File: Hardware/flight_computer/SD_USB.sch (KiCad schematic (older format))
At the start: 10 parts

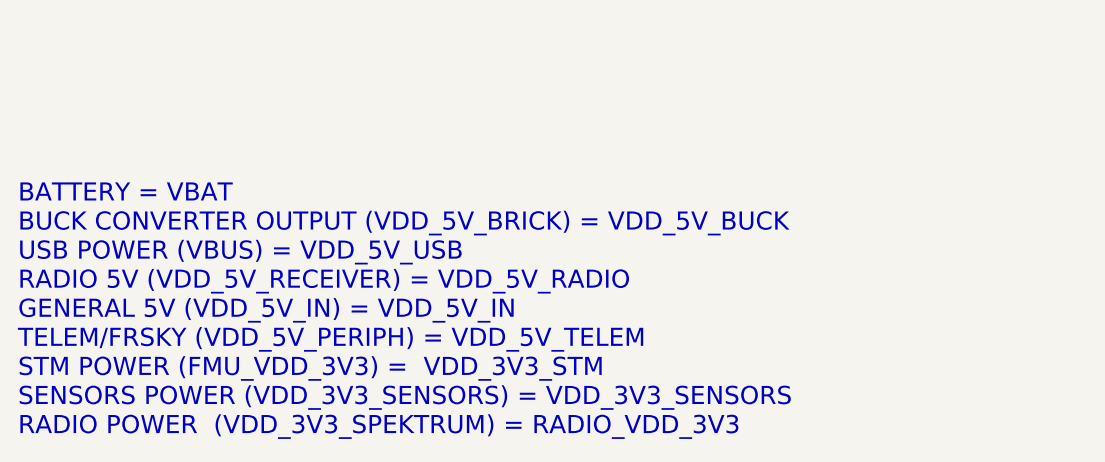
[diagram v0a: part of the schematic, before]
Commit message: added more components, added buzzer, servo circuits, re-arranged some power
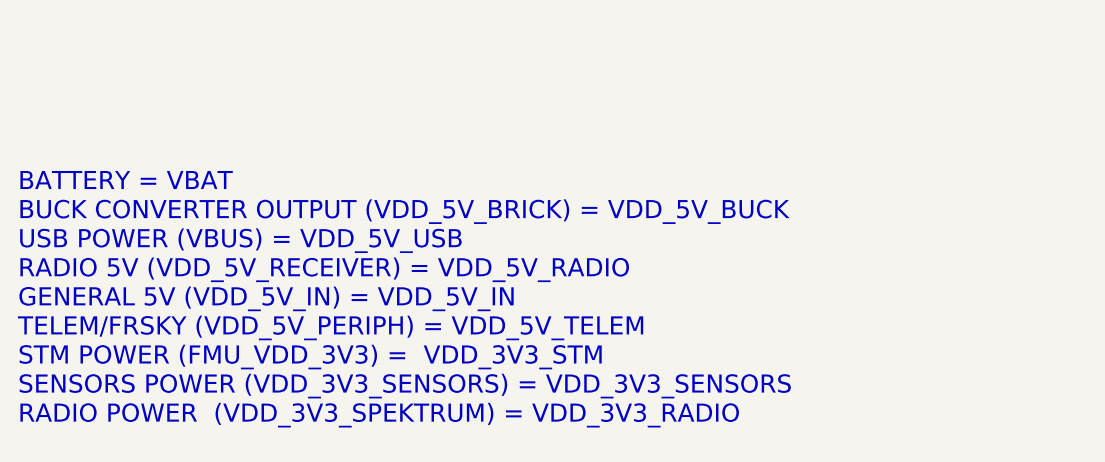
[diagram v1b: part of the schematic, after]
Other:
- note added: "BATTERY = VBAT\nBUCK CONVERTER OUTPUT (VDD_5V_BRICK) = VDD_5V_BUCK\nUSB POWER (VBUS) = VDD_5V_USB\nRADIO 5V (VDD_5V_RECEIVER) = VDD_5V_RADIO\nGENERAL 5V (VDD_5V_IN) = VDD_5V_IN\nTELEM/FRSKY (VDD_5V_PERIPH) = VDD_5V_TELEM\nSTM POWER (FMU_VDD_3V3) = VDD_3V3_STM\nSENSORS POWER (VDD_3V3_SENSORS) = VDD_3V3_SENSORS\nRADIO POWER (VDD_3V3_SPEKTRUM) = VDD_3V3_RADIO\n"
- note removed: "BATTERY = VBAT\nBUCK CONVERTER OUTPUT (VDD_5V_BRICK) = VDD_5V_BUCK\nUSB POWER (VBUS) = VDD_5V_USB\nRADIO 5V (VDD_5V_RECEIVER) = VDD_5V_RADIO\nGENERAL 5V (VDD_5V_IN) = VDD_5V_IN\nTELEM/FRSKY (VDD_5V_PERIPH) = VDD_5V_TELEM\nSTM POWER (FMU_VDD_3V3) = VDD_3V3_STM\nSENSORS POWER (VDD_3V3_SENSORS) = VDD_3V3_SENSORS\nRADIO POWER (VDD_3V3_SPEKTRUM) = RADIO_VDD_3V3\n"
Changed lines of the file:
@@
 $Descr A4 11693 8268
 encoding utf-8
-Sheet 3 5
+Sheet 2 5
 Title ""
 Date ""
@@
 	4550 1350 4600 1350
 Connection ~ 4600 1350
-Text Notes 750  7550 0    79   ~ 0
-BATTERY = VBAT\nBUCK CONVERTER OUTPUT (VDD_5V_BRICK) = VDD_5V_BUCK\nUSB POWER (VBUS) = VDD_5V_USB\nRADIO 5V (VDD_5V_RECEIVER) = VDD_5V_RADIO\nGENERAL 5V (VDD_5V_IN) = VDD_5V_IN\nTELEM/FRSKY (VDD_5V_PERIPH) = VDD_5V_TELEM\nSTM POWER (FMU_VDD_3V3) =  VDD_3V3_STM\nSENSORS POWER (VDD_3V3_SENSORS) = VDD_3V3_SENSORS\nRADIO POWER  (VDD_3V3_SPEKTRUM) = RADIO_VDD_3V3\n
+Text Notes 750  7500 0    79   ~ 0
+BATTERY = VBAT\nBUCK CONVERTER OUTPUT (VDD_5V_BRICK) = VDD_5V_BUCK\nUSB POWER (VBUS) = VDD_5V_USB\nRADIO 5V (VDD_5V_RECEIVER) = VDD_5V_RADIO\nGENERAL 5V (VDD_5V_IN) = VDD_5V_IN\nTELEM/FRSKY (VDD_5V_PERIPH) = VDD_5V_TELEM\nSTM POWER (FMU_VDD_3V3) =  VDD_3V3_STM\nSENSORS POWER (VDD_3V3_SENSORS) = VDD_3V3_SENSORS\nRADIO POWER  (VDD_3V3_SPEKTRUM) = VDD_3V3_RADIO\n
 $EndSCHEMATC
